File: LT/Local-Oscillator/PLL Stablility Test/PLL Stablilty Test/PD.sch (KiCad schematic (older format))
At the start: 25 parts

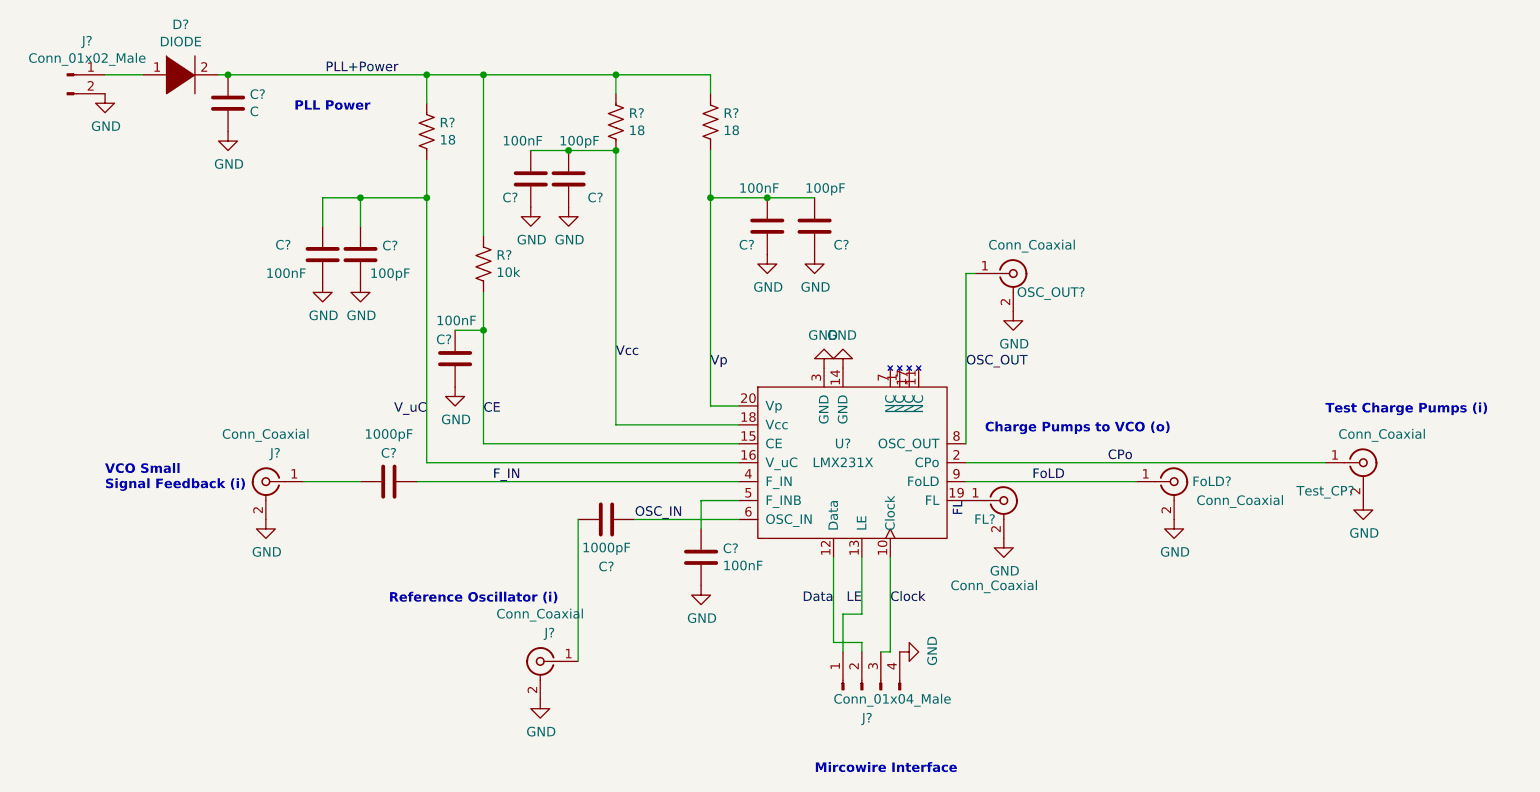
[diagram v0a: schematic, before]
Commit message: completed PLL stability test layour for individual boards
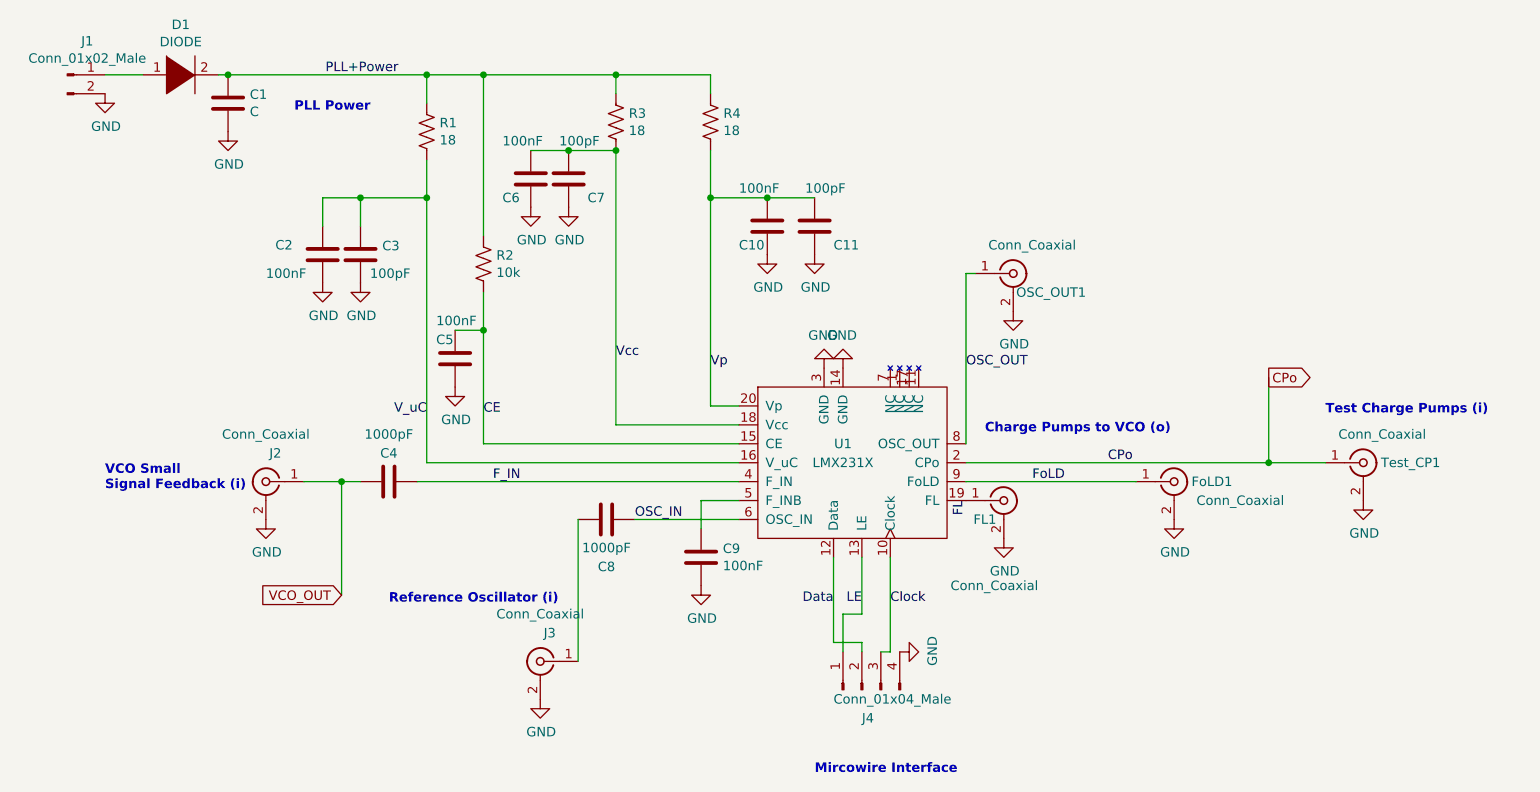
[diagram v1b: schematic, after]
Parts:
- U1: renamed from U?; footprint LMX231X:LMX231X -> LT:LMX231X
- gave numbers to parts that had none: 24
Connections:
- net VCO_OUT: now reaches C4.1, J2.1 (In)
